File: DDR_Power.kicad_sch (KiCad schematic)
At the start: 12 parts, among them U17001 NCP114AMX250TCG, U17003 Samsung K4A4G165WE-BCRC

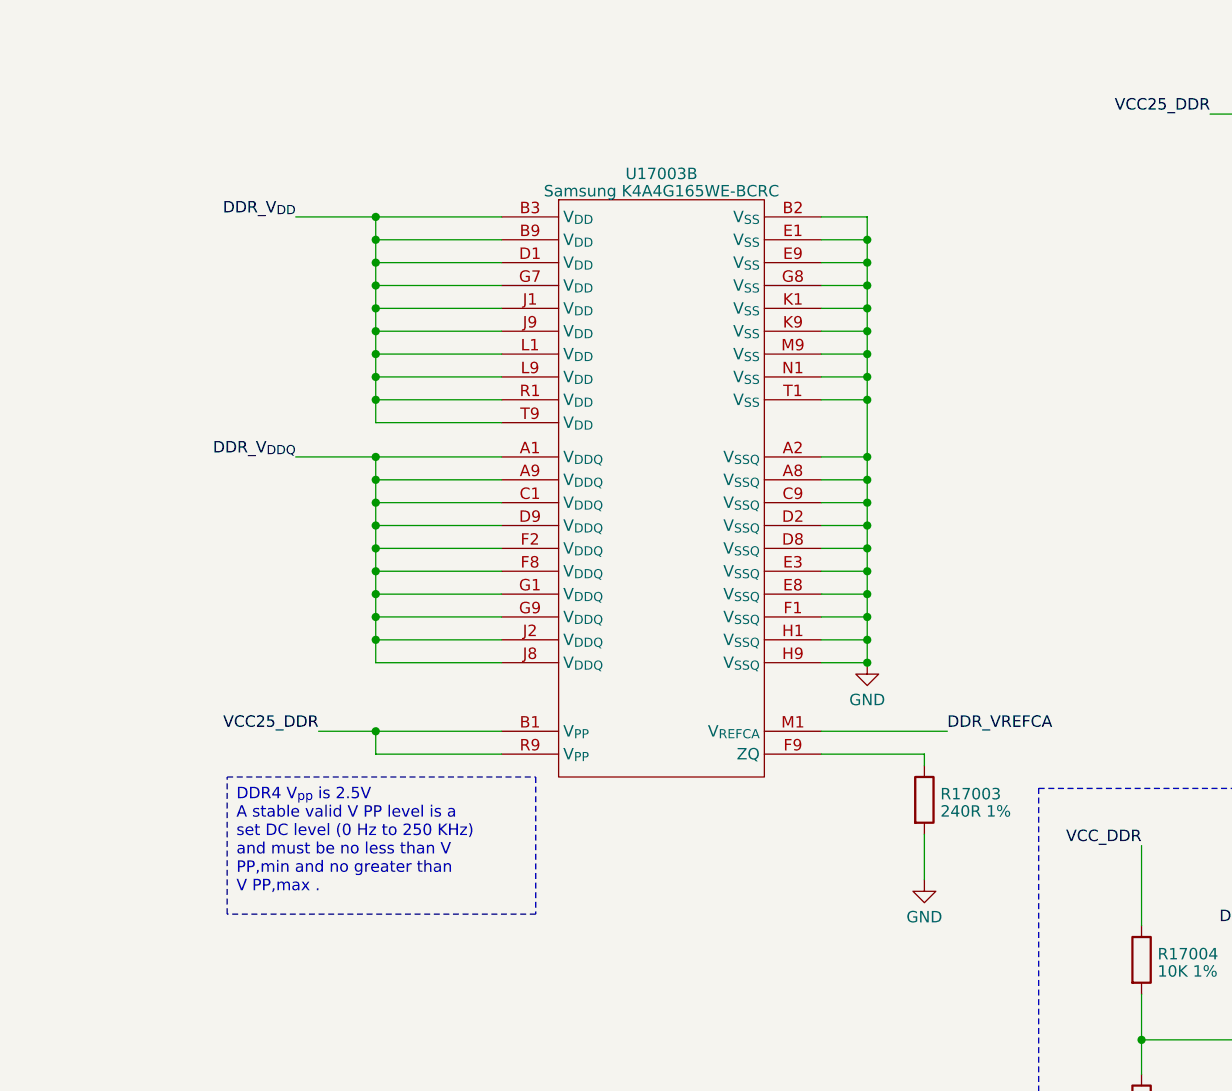
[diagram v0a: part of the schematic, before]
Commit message: remove old DDR U4B
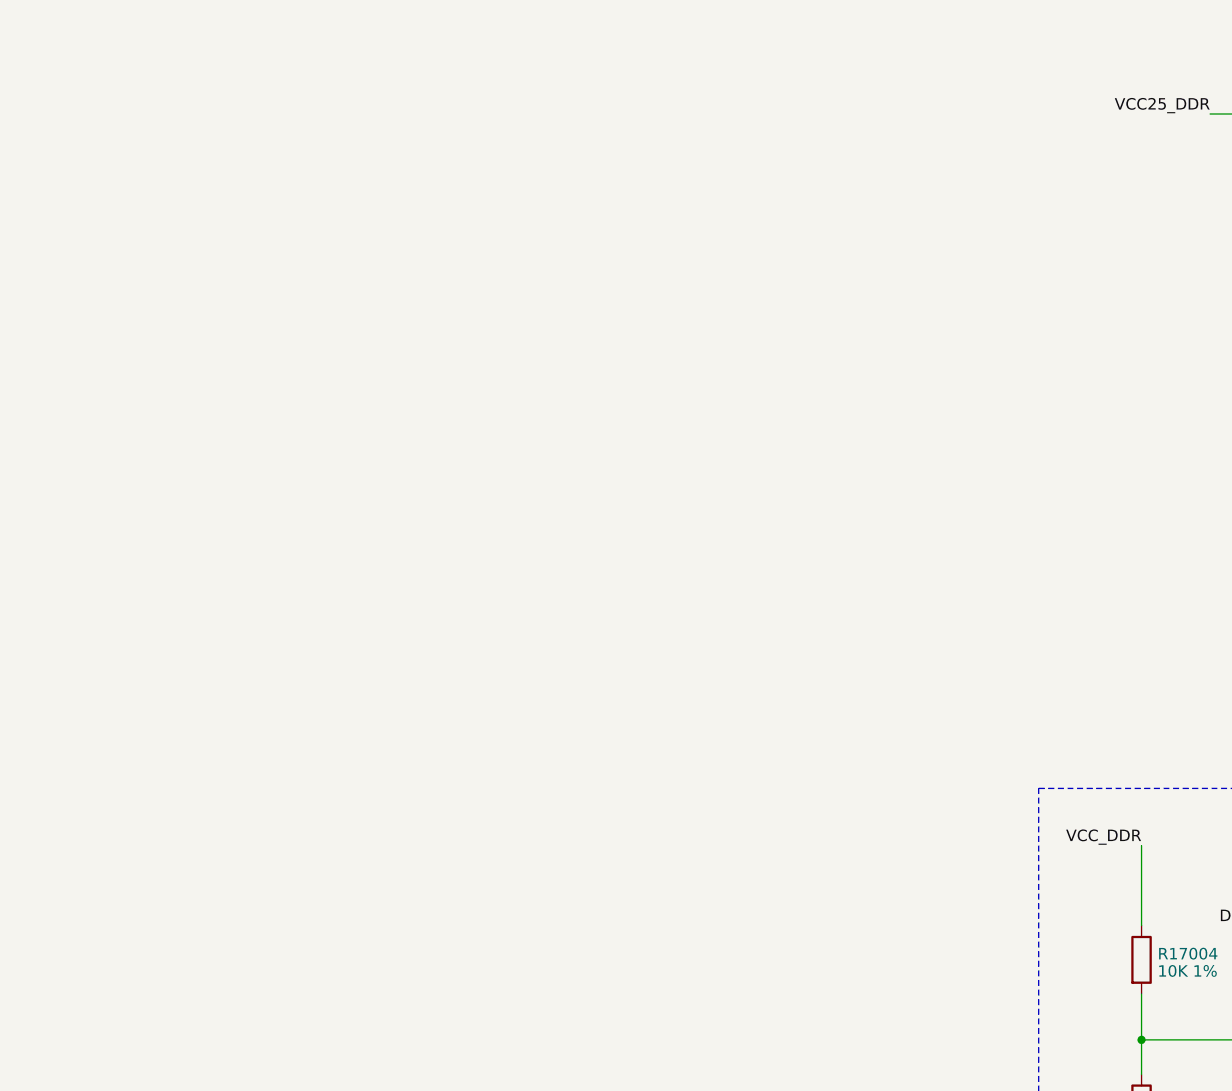
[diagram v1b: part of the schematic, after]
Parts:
- removed R17003: 240R 1%, Resistor_SMD:R_0402_1005Metric, symbol Device:R
- removed U17003: Samsung K4A4G165WE-BCRC, Package_BGA:Micron_FBGA-96_9x14mm_Layout9x16_P0.8mm, symbol Memory_DDR:Micron_DDR4_MT40A512M16TB

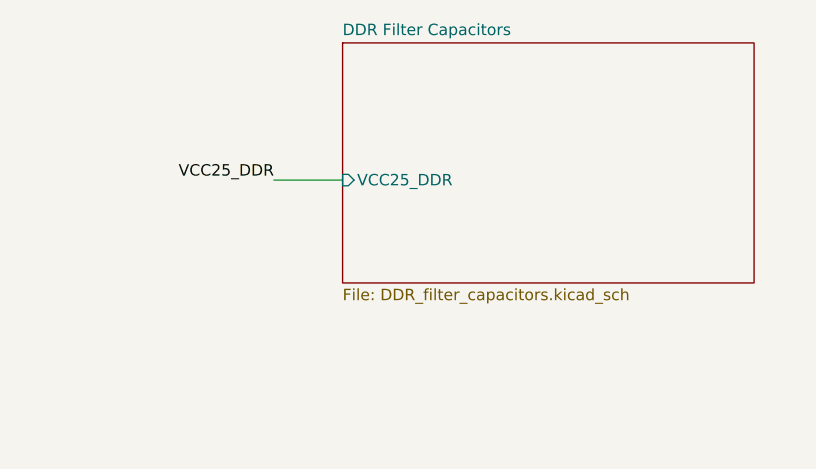
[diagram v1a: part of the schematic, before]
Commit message: move DDR capacitors into DDR4_sheet
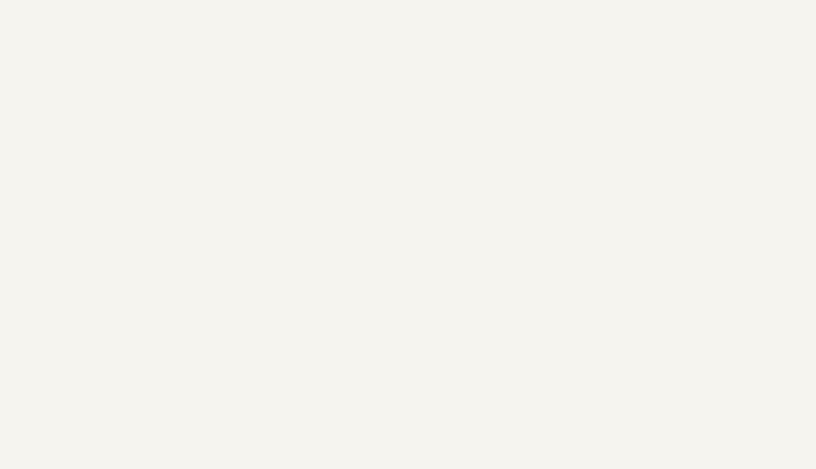
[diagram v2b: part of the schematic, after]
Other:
- removed sheet DDR Filter Capacitors
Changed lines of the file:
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@@
-    (stroke (width 0) (type default))
-  )
-  (wire (pts (xy 227.33 33.02) (xy 234.95 33.02))
     (stroke (width 0) (type default))
   )
@@
     (effects (font (size 1.27 1.27)) (justify left bottom))
   )
-  (label "VCC25_DDR" (at 227.33 33.02 180) (fields_autoplaced)
-    (effects (font (size 1.27 1.27)) (justify right bottom))
-  )
   (label "VCC_DDR" (at 72.39 22.86 180) (fields_autoplaced)
     (effects (font (size 1.27 1.27)) (justify right bottom))
@@
           (reference "R17005") (unit 1)
         )
-        (path "/e3b58043-16a3-43c8-9fad-9c9784eebfa4/9453ad46-b3ff-4d4e-8aa6-7cc75aa0f522/f6658df5-193a-49b6-ab60-4ac3c0bbbc45/b7d33089-b835-4c65-840f-b2075d1befa5"
-          (reference "R?") (unit 1)
-        )
       )
     )
@@
         (path "/e3b58043-16a3-43c8-9fad-9c9784eebfa4/9453ad46-b3ff-4d4e-8aa6-7cc75aa0f522/f6658df5-193a-49b6-ab60-4ac3c0bbbc45"
           (reference "R17004") (unit 1)
-        )
-        (path "/e3b58043-16a3-43c8-9fad-9c9784eebfa4/9453ad46-b3ff-4d4e-8aa6-7cc75aa0f522/f6658df5-193a-49b6-ab60-4ac3c0bbbc45/b7d33089-b835-4c65-840f-b2075d1befa5"
-          (reference "R?") (unit 1)
         )
       )
@@
           (reference "C17005") (unit 1)
         )
-        (path "/e3b58043-16a3-43c8-9fad-9c9784eebfa4/9453ad46-b3ff-4d4e-8aa6-7cc75aa0f522/f6658df5-193a-49b6-ab60-4ac3c0bbbc45/b7d33089-b835-4c65-840f-b2075d1befa5"
-          (reference "C?") (unit 1)
-        )
       )
     )
@@
         (path "/e3b58043-16a3-43c8-9fad-9c9784eebfa4/9453ad46-b3ff-4d4e-8aa6-7cc75aa0f522/f6658df5-193a-49b6-ab60-4ac3c0bbbc45"
           (reference "#PWR017011") (unit 1)
-        )
-        (path "/e3b58043-16a3-43c8-9fad-9c9784eebfa4/9453ad46-b3ff-4d4e-8aa6-7cc75aa0f522/f6658df5-193a-49b6-ab60-4ac3c0bbbc45/b7d33089-b835-4c65-840f-b2075d1befa5"
-          (reference "#PWR?") (unit 1)
         )
       )
@@
           (reference "C17003") (unit 1)
         )
-        (path "/e3b58043-16a3-43c8-9fad-9c9784eebfa4/9453ad46-b3ff-4d4e-8aa6-7cc75aa0f522/f6658df5-193a-49b6-ab60-4ac3c0bbbc45/b7d33089-b835-4c65-840f-b2075d1befa5"
-          (reference "C?") (unit 1)
-        )
       )
     )
@@
           (reference "#PWR017008") (unit 1)
         )
-        (path "/e3b58043-16a3-43c8-9fad-9c9784eebfa4/9453ad46-b3ff-4d4e-8aa6-7cc75aa0f522/f6658df5-193a-49b6-ab60-4ac3c0bbbc45/b7d33089-b835-4c65-840f-b2075d1befa5"
-          (reference "#PWR?") (unit 1)
-        )
       )
     )
@@
           (reference "#PWR017009") (unit 1)
         )
-        (path "/e3b58043-16a3-43c8-9fad-9c9784eebfa4/9453ad46-b3ff-4d4e-8aa6-7cc75aa0f522/f6658df5-193a-49b6-ab60-4ac3c0bbbc45/b7d33089-b835-4c65-840f-b2075d1befa5"
-          (reference "#PWR?") (unit 1)
-        )
       )
     )
@@
         (path "/e3b58043-16a3-43c8-9fad-9c9784eebfa4/9453ad46-b3ff-4d4e-8aa6-7cc75aa0f522/f6658df5-193a-49b6-ab60-4ac3c0bbbc45"
           (reference "#PWR017012") (unit 1)
-        )
-        (path "/e3b58043-16a3-43c8-9fad-9c9784eebfa4/9453ad46-b3ff-4d4e-8aa6-7cc75aa0f522/f6658df5-193a-49b6-ab60-4ac3c0bbbc45/b7d33089-b835-4c65-840f-b2075d1befa5"
-          (reference "#PWR?") (unit 1)
         )
       )
@@
           (reference "C17006") (unit 1)
         )
-        (path "/e3b58043-16a3-43c8-9fad-9c9784eebfa4/9453ad46-b3ff-4d4e-8aa6-7cc75aa0f522/f6658df5-193a-49b6-ab60-4ac3c0bbbc45/b7d33089-b835-4c65-840f-b2075d1befa5"
-          (reference "C?") (unit 1)
-        )
       )
     )
@@
           (reference "C17004") (unit 1)
         )
-        (path "/e3b58043-16a3-43c8-9fad-9c9784eebfa4/9453ad46-b3ff-4d4e-8aa6-7cc75aa0f522/f6658df5-193a-49b6-ab60-4ac3c0bbbc45/b7d33089-b835-4c65-840f-b2075d1befa5"
-          (reference "C?") (unit 1)
-        )
       )
     )
@@
           (reference "#PWR017010") (unit 1)
         )
-        (path "/e3b58043-16a3-43c8-9fad-9c9784eebfa4/9453ad46-b3ff-4d4e-8aa6-7cc75aa0f522/f6658df5-193a-49b6-ab60-4ac3c0bbbc45/b7d33089-b835-4c65-840f-b2075d1befa5"
-          (reference "#PWR?") (unit 1)
-        )
-      )
-    )
-  )
-  (sheet (at 234.95 17.78) (size 45.72 26.67) (fields_autoplaced)
-    (stroke (width 0.1524) (type solid))
-    (fill (color 0 0 0 0.0000))
-    (property "Sheetname" "DDR Filter Capacitors" (at 234.95 17.0684 0)
-      (effects (font (size 1.27 1.27)) (justify left bottom))
-    )
-    (property "Sheetfile" "DDR_filter_capacitors.kicad_sch" (at 234.95 45.0346 0)
-      (effects (font (size 1.27 1.27)) (justify left top))
-    )
-    (pin "VCC25_DDR" input (at 234.95 33.02 180)
-      (effects (font (size 1.27 1.27)) (justify left))
-    )
-    (instances
-      (project "leaf"
-        (path "/e3b58043-16a3-43c8-9fad-9c9784eebfa4/9453ad46-b3ff-4d4e-8aa6-7cc75aa0f522/f6658df5-193a-49b6-ab60-4ac3c0bbbc45" (page "19"))
-      )
-    )
+      )
+    )
